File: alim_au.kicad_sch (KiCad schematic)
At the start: 30 parts, among them U1 AMS1117-3.3

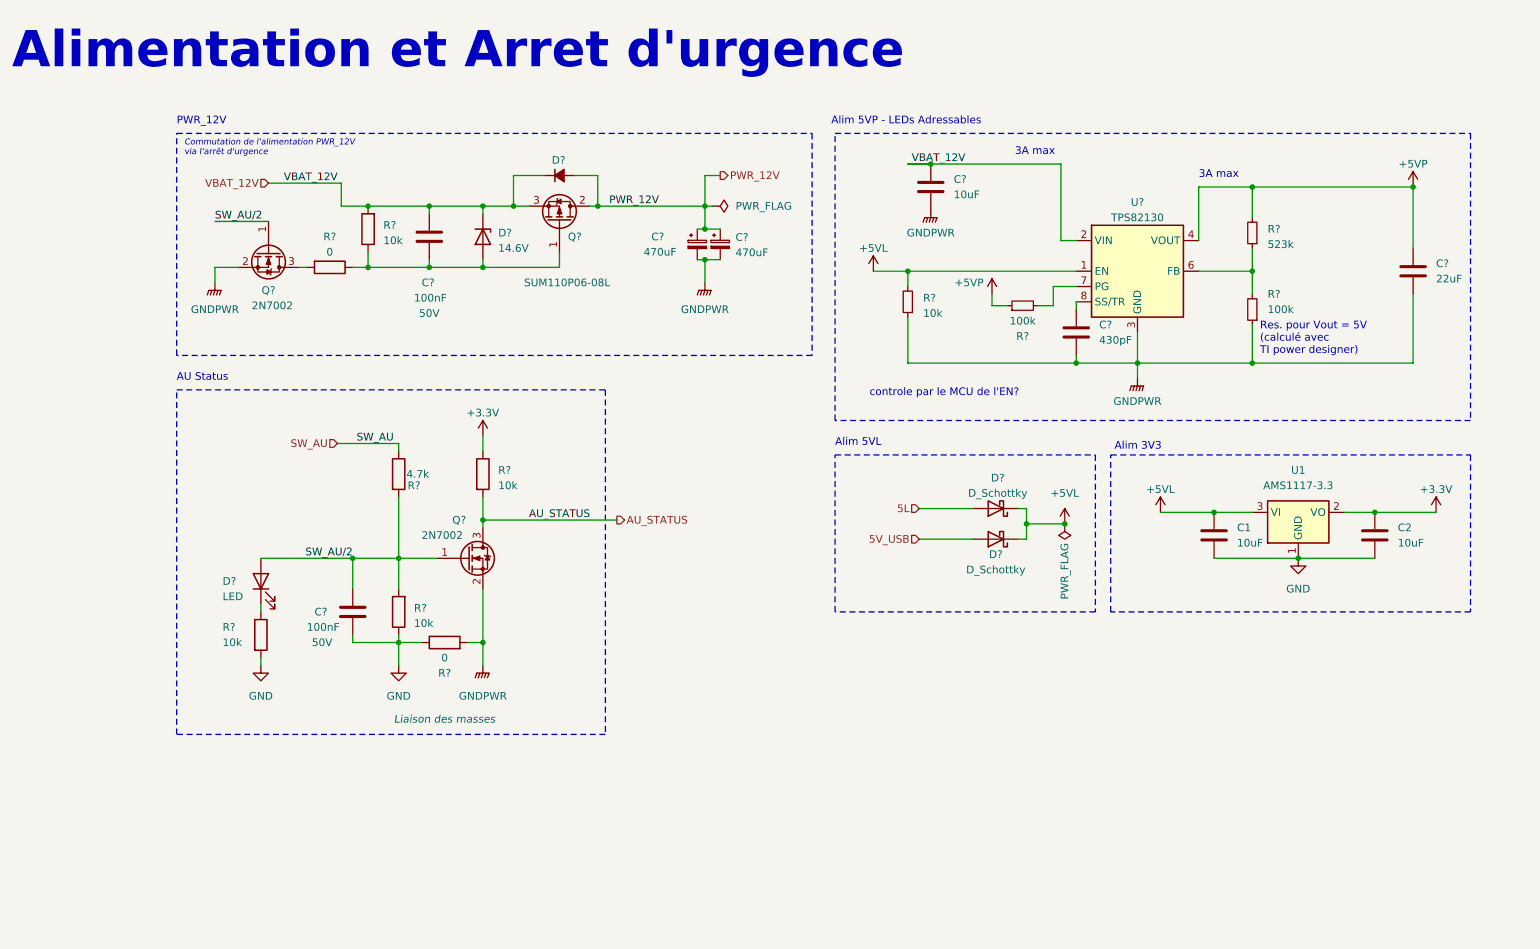
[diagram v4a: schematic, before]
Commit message: optimisation empreinte passif (TODO fp diode), TODO ajouter LED temoin diverse, groupement sur PCB des nouveaux composant
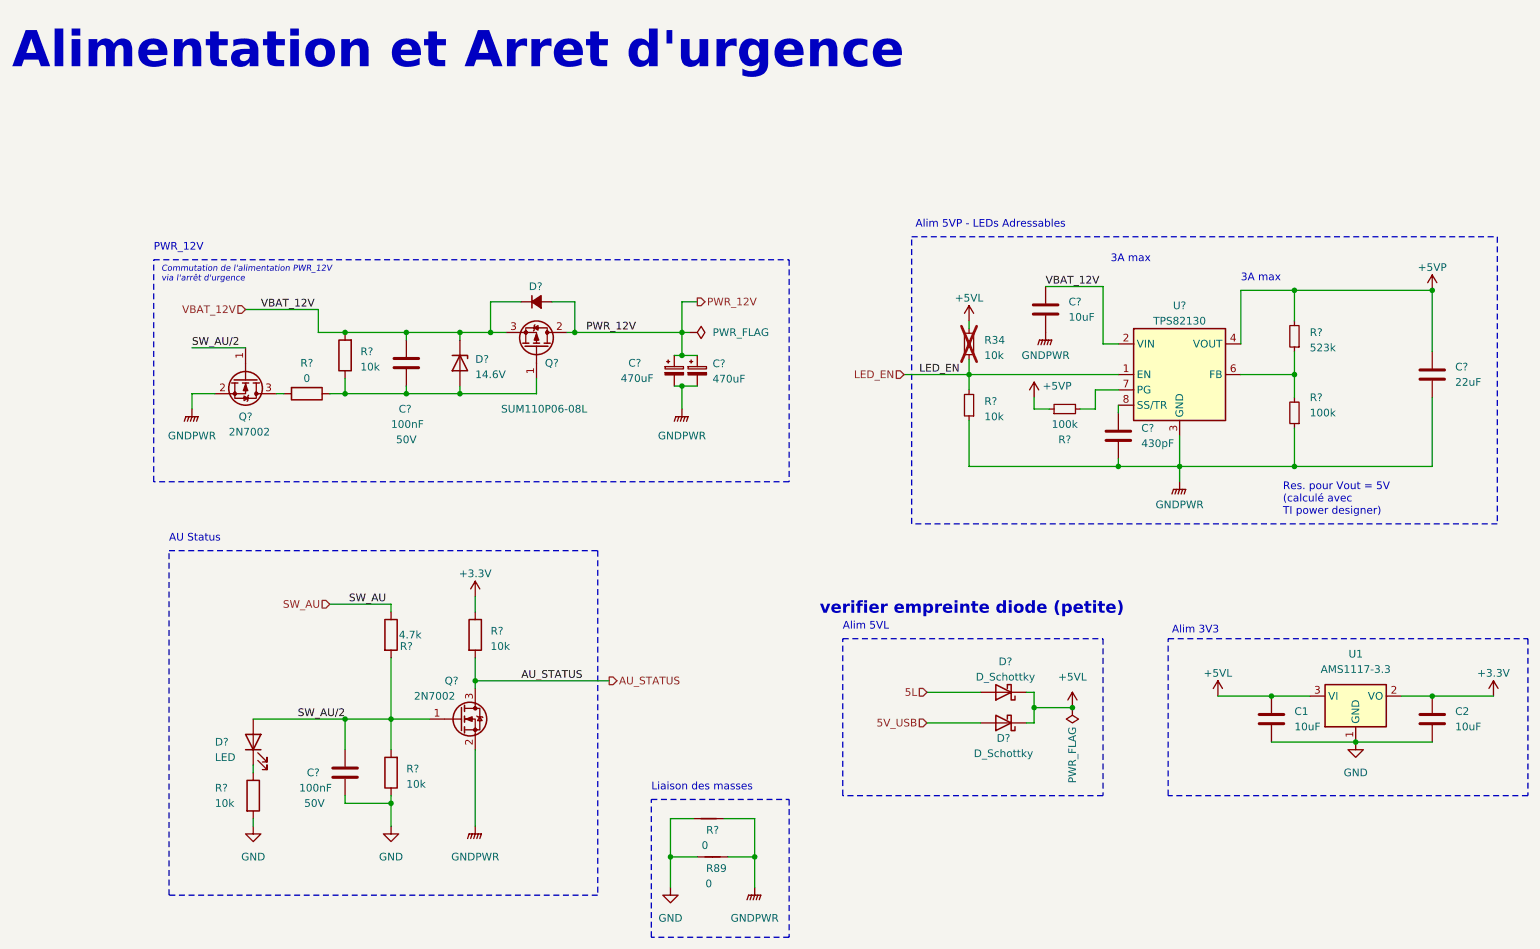
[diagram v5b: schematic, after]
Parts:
- added R34: 10k, Resistor_SMD:R_0603_1608Metric, symbol Device:R_Small
- added R89: 0, NetTie:NetTie-2_SMD_Pad0.5mm, symbol Device:NetTie_2
- R?: footprint Resistor_SMD:R_0603_1608Metric -> Resistor_SMD:R_0402_1005Metric
- R?: footprint Capacitor_SMD:C_0603_1608Metric -> NetTie:NetTie-2_SMD_Pad0.5mm; symbol Device:R -> Device:NetTie_2; now left out of the parts list
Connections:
- net +5VL: now also R34.2; no longer R?.2, U?.1 (EN)
- net GND: now also R?.2, R89.2; no longer R?.1
- net GNDPWR: now also R?.1, R89.1; no longer R?.2
- new net LED_EN: R34.1, R?.2, U?.1 (EN)
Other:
- note added: "Liaison des masses"
- note added: "verifier empreinte diode (petite)"
- note removed: "controle par le MCU de l'EN?"
- moved on the sheet: C1, C2, C?, D?, Q?, R?, U1, U?

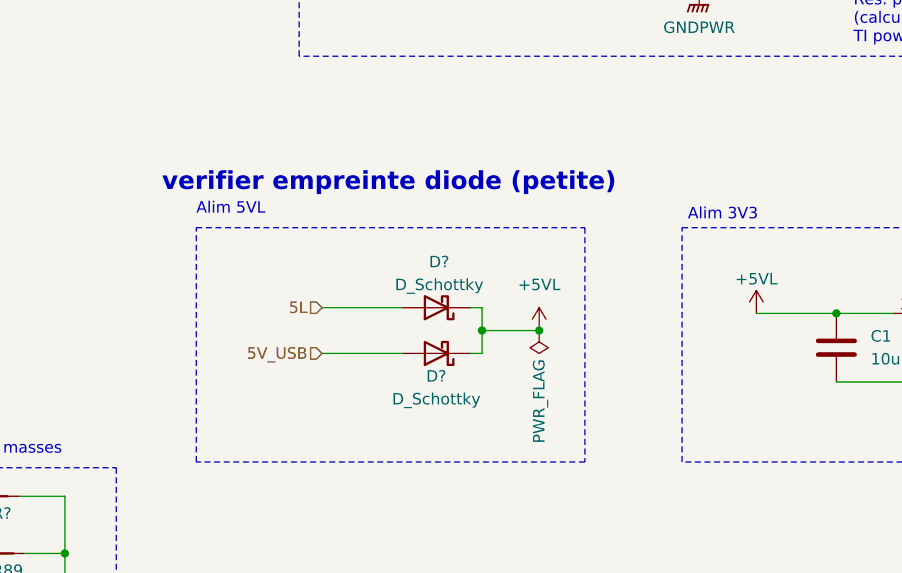
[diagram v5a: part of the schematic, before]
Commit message: placement en cours, remplacement diode schotcky, customisation empreinte capteur pression, suppression R pour les signaux figé du uC (SW, BOOT, etc). TODO avancer placement, ajouter LED
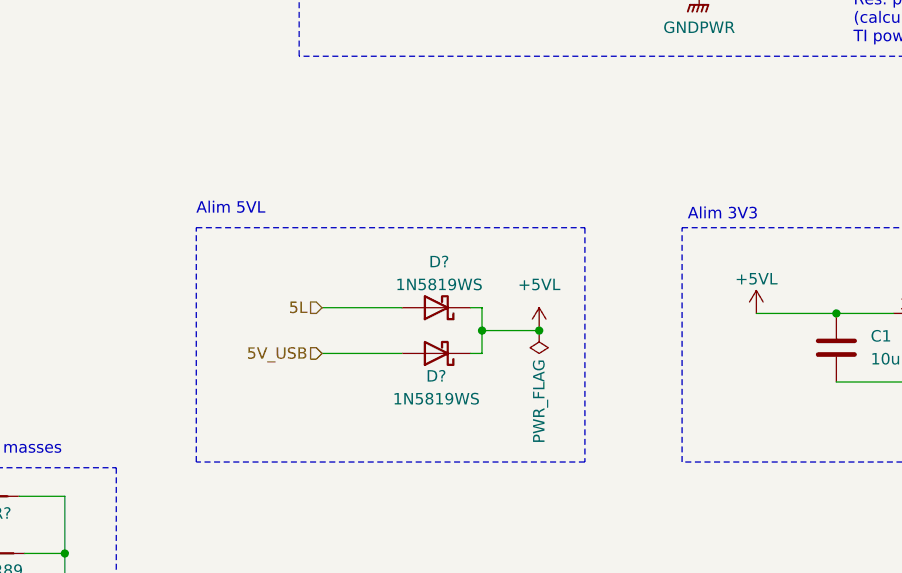
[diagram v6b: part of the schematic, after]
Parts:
- D? (x2): value D_Schottky -> 1N5819WS; footprint Diode_SMD:D_SOD-882 -> Diode_SMD:D_SOD-323_HandSoldering; JLCPCB (none) -> C191023
- D?: footprint Diode_SMD:D_SOD-323 -> Diode_SMD:D_SOD-323_HandSoldering
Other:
- note removed: "verifier empreinte diode (petite)"
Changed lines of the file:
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@@
-		)
-	)
-	(text "verifier empreinte diode (petite)"
-		(exclude_from_sim no)
-		(at 149.225 114.3 0)
-		(effects
-			(font
-				(size 2 2)
-				(thickness 0.4)
-				(bold yes)
-				(color 255 0 0 1)
-			)
-			(justify left bottom)
 		)
 	)
@@
 			)
 		)
-		(property "Value" "D_Schottky"
+		(property "Value" "1N5819WS"
 			(at 179.705 137.16 0)
 			(effects
@@
 			)
 		)
-		(property "Footprint" "Diode_SMD:D_SOD-882"
+		(property "Footprint" "Diode_SMD:D_SOD-323_HandSoldering"
 			(at 179.705 132.08 0)
 			(effects
@@
 		)
 		(property "Description" ""
+			(at 179.705 132.08 0)
+			(effects
+				(font
+					(size 1.27 1.27)
+				)
+				(hide yes)
+			)
+		)
+		(property "JLCPCB" "C191023"
 			(at 179.705 132.08 0)
 			(effects
@@
 			)
 		)
-		(property "Value" "D_Schottky"
+		(property "Value" "1N5819WS"
 			(at 180.0225 124.46 0)
 			(effects
@@
 			)
 		)
-		(property "Footprint" "Diode_SMD:D_SOD-882"
+		(property "Footprint" "Diode_SMD:D_SOD-323_HandSoldering"
 			(at 179.705 127 0)
 			(effects
@@
 		)
 		(property "Description" ""
+			(at 179.705 127 0)
+			(effects
+				(font
+					(size 1.27 1.27)
+				)
+				(hide yes)
+			)
+		)
+		(property "JLCPCB" "C191023"
 			(at 179.705 127 0)
 			(effects
@@
 			)
 		)
-		(property "Footprint" "Diode_SMD:D_SOD-323"
+		(property "Footprint" "Diode_SMD:D_SOD-323_HandSoldering"
 			(at 89.535 72.39 0)
 			(effects

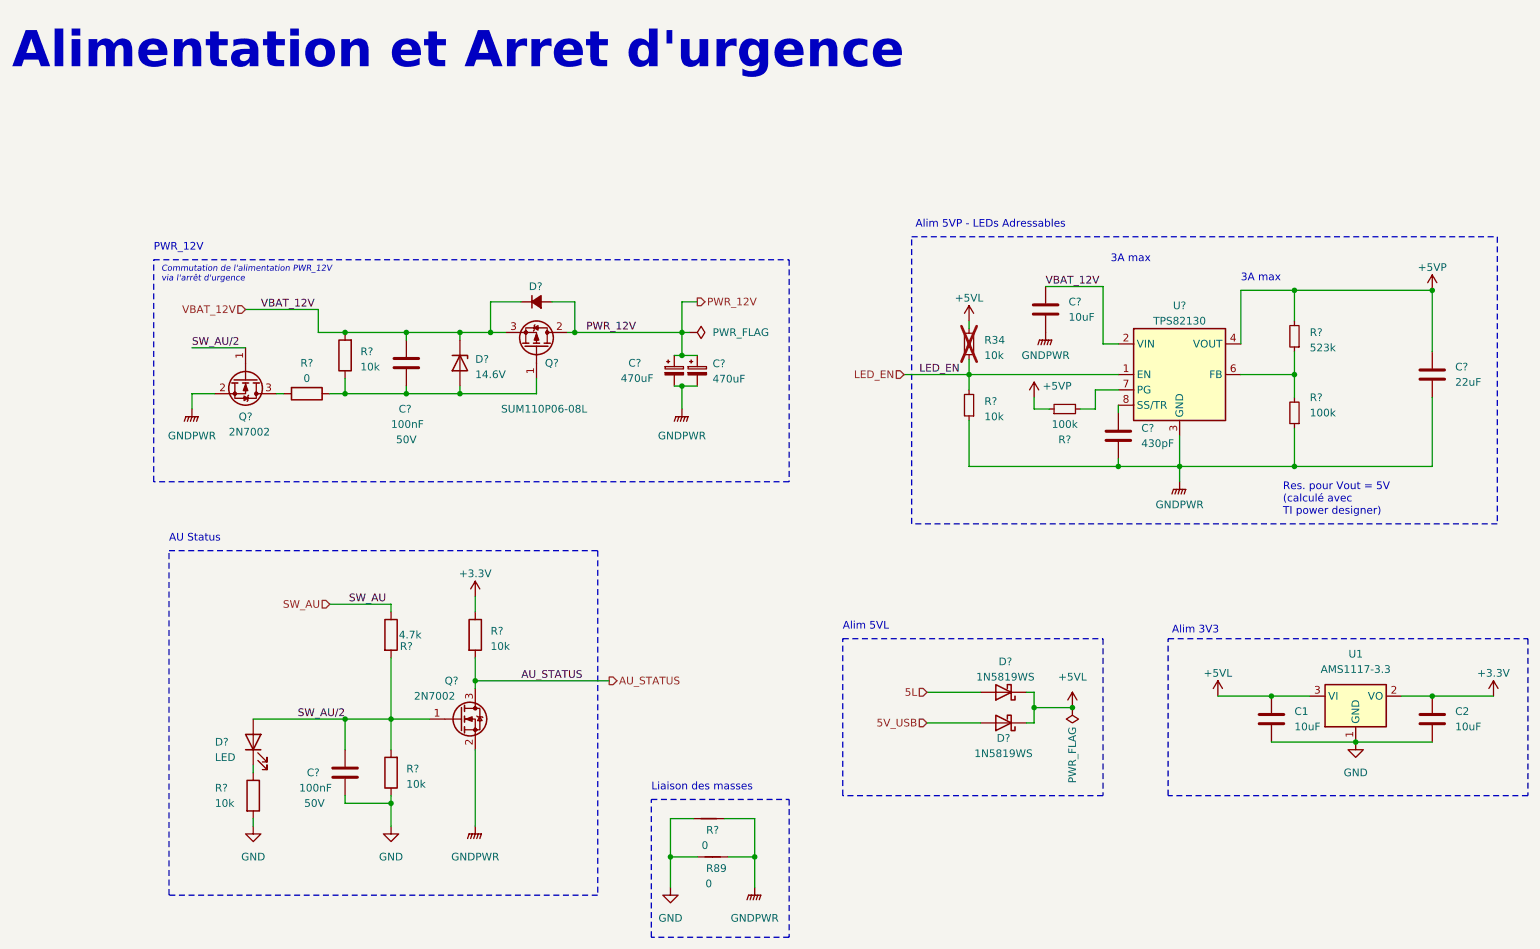
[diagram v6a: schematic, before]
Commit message: ajout regle routage JLCPCB, fin placement grossier et debut reassignation. ajout de led temoin, homogeinisation empreinte passif et remplacement 0ohm par empreintre jumper PCB 0402.
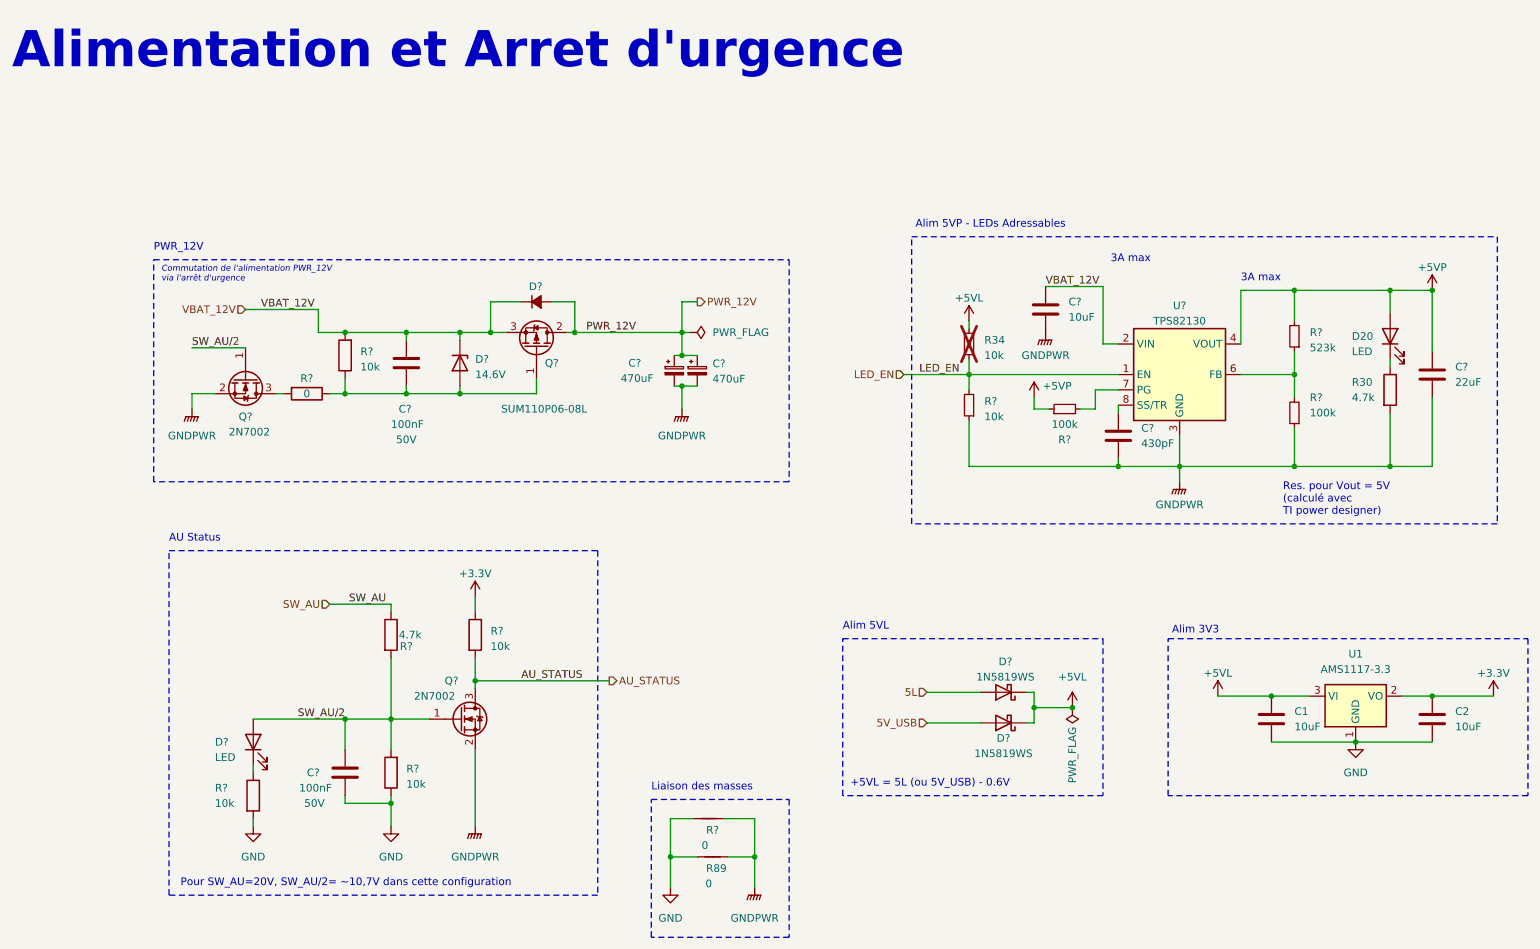
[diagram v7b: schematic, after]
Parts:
- added D20: LED, LED_SMD:LED_0603_1608Metric, symbol Device:LED
- added R30: 4.7k, Resistor_SMD:R_0603_1608Metric, symbol Device:R
- C1, C2, C?: footprint Capacitor_SMD:C_0603_1608Metric -> Capacitor_SMD:C_0805_2012Metric
- R?: footprint Resistor_SMD:R_0402_1005Metric -> 12V-actuators_pcb:R_0402_1005Metric_jumperClosed; now left out of the parts list
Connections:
- net +5VP: now also D20.2 (A)
- net GNDPWR: now also R30.2
- new net: D20.1 (K), R30.1
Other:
- note added: "+5VL = 5L (ou 5V_USB) - 0.6V"
- note added: "Pour SW_AU=20V, SW_AU/2= ~10,7V dans cette configuration"
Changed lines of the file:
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@@
 	)
 	(junction
+		(at 243.84 60.325)
+		(diameter 0)
+		(color 0 0 0 0)
+	)
+	(junction
 		(at 250.825 60.325)
 		(diameter 0)
@@
 	)
 	(junction
+		(at 243.84 89.535)
+		(diameter 0)
+		(color 0 0 0 0)
+	)
+	(junction
 		(at 227.965 89.535)
 		(diameter 0)
@@
 	(wire
 		(pts
-			(xy 227.965 89.535) (xy 250.825 89.535)
+			(xy 227.965 89.535) (xy 243.84 89.535)
 		)
 		(stroke
@@
 	(wire
 		(pts
+			(xy 243.84 60.325) (xy 250.825 60.325)
+		)
+		(stroke
+			(width 0)
+			(type default)
+		)
+	)
+	(wire
+		(pts
 			(xy 173.99 74.295) (xy 173.99 76.835)
 		)
@@
 	(wire
 		(pts
+			(xy 243.84 71.755) (xy 243.84 73.025)
+		)
+		(stroke
+			(width 0)
+			(type default)
+		)
+	)
+	(wire
+		(pts
 			(xy 92.075 121.285) (xy 92.075 125.095)
 		)
@@
 	(wire
 		(pts
-			(xy 227.965 60.325) (xy 250.825 60.325)
+			(xy 227.965 60.325) (xy 243.84 60.325)
 		)
 		(stroke
@@
 	(wire
 		(pts
+			(xy 243.84 80.645) (xy 243.84 89.535)
+		)
+		(stroke
+			(width 0.5)
+			(type default)
+			(color 0 0 0 1)
+		)
+	)
+	(wire
+		(pts
 			(xy 126.365 62.23) (xy 126.365 67.31)
 		)
@@
 	(wire
 		(pts
+			(xy 243.84 60.325) (xy 243.84 64.135)
+		)
+		(stroke
+			(width 0)
+			(type default)
+		)
+	)
+	(wire
+		(pts
 			(xy 124.46 154.305) (xy 128.905 154.305)
 		)
@@
 	(wire
 		(pts
+			(xy 243.84 89.535) (xy 250.825 89.535)
+		)
+		(stroke
+			(width 0.5)
+			(type default)
+			(color 0 0 0 1)
+		)
+	)
+	(wire
+		(pts
 			(xy 55.245 139.065) (xy 55.245 140.335)
 		)
@@
 		)
 	)
+	(text "Pour SW_AU=20V, SW_AU/2= ~10,7V dans cette configuration"
+		(exclude_from_sim no)
+		(at 43.18 159.385 0)
+		(effects
+			(font
+				(size 1.27 1.27)
+			)
+			(justify left bottom)
+		)
+	)
 	(text "Commutation de l'alimentation PWR_12V\nvia l'arrêt d'urgence"
 		(exclude_from_sim no)
@@
 		)
 	)
+	(text "+5VL = 5L (ou 5V_USB) - 0.6V"
+		(exclude_from_sim no)
+		(at 154.305 142.875 0)
+		(effects
+			(font
+				(size 1.27 1.27)
+			)
+			(justify left bottom)
+		)
+	)
 	(label "SW_AU{slash}2"
 		(at 70.485 131.445 180)
@@
 	)
 	(symbol
+		(lib_id "Device:R")
+		(at 243.84 76.835 0)
+		(unit 1)
+		(exclude_from_sim no)
+		(in_bom yes)
+		(on_board yes)
+		(dnp no)
+		(property "Reference" "R30"
+			(at 237.49 75.565 0)
+			(effects
+				(font
+					(size 1.27 1.27)
+				)
+				(justify left)
+			)
+		)
+		(property "Value" "4.7k"
+			(at 237.49 78.105 0)
+			(effects
+				(font
+					(size 1.27 1.27)
+				)
+				(justify left)
+			)
+		)
+		(property "Footprint" "Resistor_SMD:R_0603_1608Metric"
+			(at 242.062 76.835 90)
+			(effects
+				(font
+					(size 1.27 1.27)
+				)
+				(hide yes)
+			)
+		)
+		(property "Datasheet" "~"
+			(at 243.84 76.835 0)
+			(effects
+				(font
+					(size 1.27 1.27)
+				)
+				(hide yes)
+			)
+		)
+		(property "Description" ""
+			(at 243.84 76.835 0)
+			(effects
+				(font
+					(size 1.27 1.27)
+				)
+				(hide yes)
+			)
+		)
+		(pin "1"
+		)
+		(pin "2"
+		)
+		(instances
+			(project "12v-actuators-pcb"
+				(path "/d0b6cc72-ff07-4f5e-a148-04b65c86a715/a9998e65-7bac-4337-98c8-7de7c845405f"
+					(reference "R30")
+					(unit 1)
+				)
+			)
+		)
+	)
+	(symbol
 		(lib_id "Device:D_Schottky")
 		(at 179.705 127 180)
@@
 		(unit 1)
 		(exclude_from_sim no)
-		(in_bom yes)
+		(in_bom no)
 		(on_board yes)
 		(dnp no)
-		(fields_autoplaced yes)
 		(property "Reference" "R?"
-			(at 64.135 72.39 90)
+			(at 64.135 74.93 90)
 			(effects
 				(font
@@
 		)
 		(property "Value" "0"
-			(at 64.135 74.93 90)
+			(at 64.135 77.47 90)
 			(effects
 				(font
@@
 			)
 		)
-		(property "Footprint" "Resistor_SMD:R_0402_1005Metric"
+		(property "Footprint" "12V-actuators_pcb:R_0402_1005Metric_jumperClosed"
 			(at 64.135 75.692 90)
 			(effects
@@
 			)
 		)
-		(property "Footprint" "Capacitor_SMD:C_0603_1608Metric"
+		(property "Footprint" "Capacitor_SMD:C_0805_2012Metric"
 			(at 187.6552 67.31 0)
 			(effects
@@
 			)
 		)
-		(property "Footprint" "Capacitor_SMD:C_0603_1608Metric"
+		(property "Footprint" "Capacitor_SMD:C_0805_2012Metric"
 			(at 251.7902 135.255 0)
 			(effects
@@
 	)
 	(symbol
+		(lib_id "Device:LED")
+		(at 243.84 67.945 90)
+		(unit 1)
+		(exclude_from_sim no)
+		(in_bom yes)
+		(on_board yes)
+		(dnp no)
+		(property "Reference" "D20"
+			(at 237.49 67.945 90)
+			(effects
+				(font
+					(size 1.27 1.27)
+				)
+				(justify right)
+			)
+		)
+		(property "Value" "LED"
+			(at 237.49 70.485 90)
+			(effects
+				(font
+					(size 1.27 1.27)
+				)
+				(justify right)
+			)
+		)
+		(property "Footprint" "LED_SMD:LED_0603_1608Metric"
+			(at 243.84 67.945 0)
+			(effects
+				(font
+					(size 1.27 1.27)
+				)
+				(hide yes)
+			)
+		)
+		(property "Datasheet" "~"
+			(at 243.84 67.945 0)
+			(effects
+				(font
+					(size 1.27 1.27)
+				)
+				(hide yes)
+			)
+		)
+		(property "Description" ""
+			(at 243.84 67.945 0)
+			(effects
+				(font
+					(size 1.27 1.27)
+				)
+				(hide yes)
+			)
+		)
+		(pin "1"
+		)
+		(pin "2"
+		)
+		(instances
+			(project "12v-actuators-pcb"
+				(path "/d0b6cc72-ff07-4f5e-a148-04b65c86a715/a9998e65-7bac-4337-98c8-7de7c845405f"
+					(reference "D20")
+					(unit 1)
+				)
+			)
+		)
+	)
+	(symbol
 		(lib_id "Device:R")
 		(at 78.105 117.475 0)
@@
 			)
 		)
-		(property "Footprint" "Capacitor_SMD:C_0603_1608Metric"
+		(property "Footprint" "Capacitor_SMD:C_0805_2012Metric"
 			(at 225.1202 135.255 0)
 			(effects
